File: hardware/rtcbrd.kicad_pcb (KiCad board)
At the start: 2 copper layers, 11 x 11 mm, 15 parts, among them J1 02x04, Q1 SI2302, Q2 AO3407, U1 PCF8563TS, Y1 32.768kHz

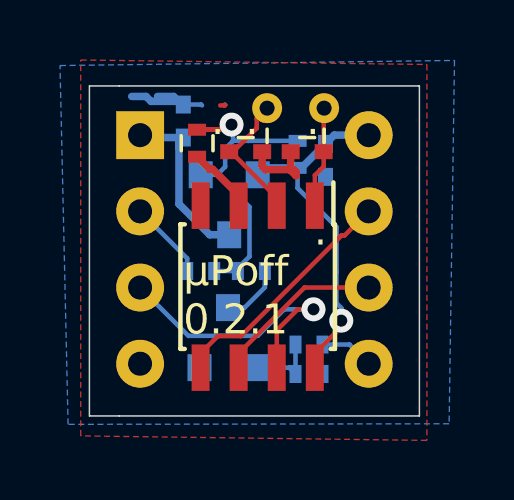
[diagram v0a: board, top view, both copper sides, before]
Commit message: Add I²C Pull-Up; Move value markings
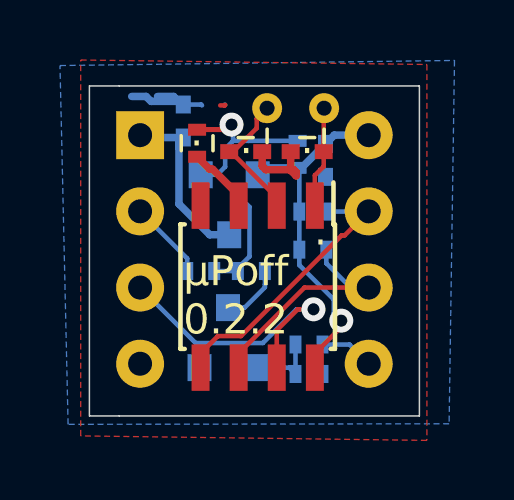
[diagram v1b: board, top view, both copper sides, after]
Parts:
- added R7: 1.2kΩ, Resistors_SMD:R_0402, B.Cu at (62.7, 34.8)
- added R8: 1.2kΩ, Resistors_SMD:R_0402, B.Cu at (62.7, 36.1)
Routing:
- net SCL: track 5.72 -> 7.92 mm
- net SDA: track 8.04 -> 9.46 mm
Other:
- board text added: "µPoff 0.2.2"
- board text removed: "µPoff 0.2.1"
